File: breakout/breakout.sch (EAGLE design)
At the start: 34 parts, among them X1 PCIE-MINI-CONN

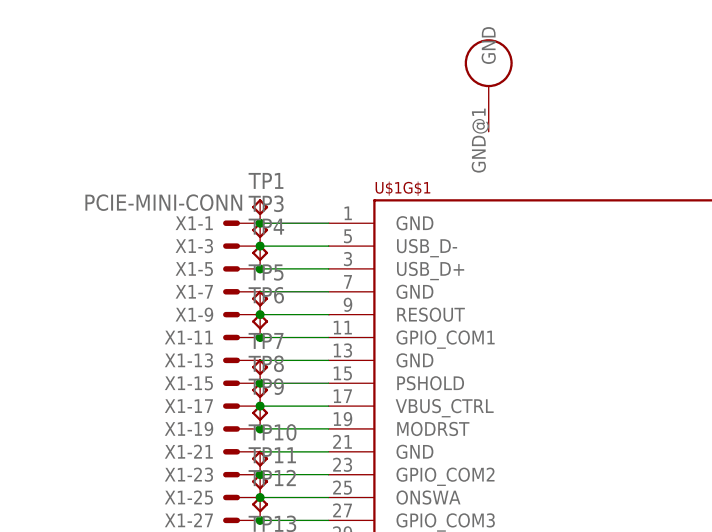
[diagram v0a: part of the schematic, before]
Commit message: Fix incorrect signal in breakout board
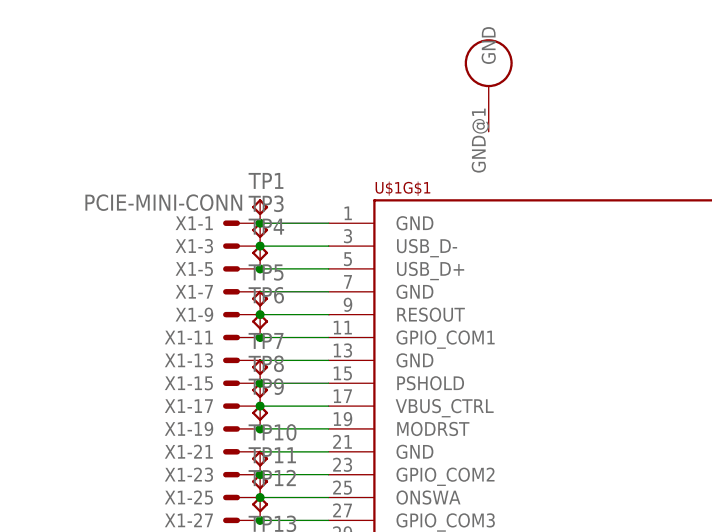
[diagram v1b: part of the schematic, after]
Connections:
- net USB_D+ renamed USB_P
- net USB_D- renamed USB_N
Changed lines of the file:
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@@
 </busses>
 <nets>
-<net name="USB_D-" class="0">
-<segment>
-<pinref part="X1" gate="-3" pin="S"/>
-<pinref part="U$1" gate="G$1" pin="USB_D-"/>
-<wire x1="25.4" y1="68.58" x2="33.02" y2="68.58" width="0.1524" layer="91"/>
-<pinref part="TP3" gate="G$1" pin="TP"/>
-<junction x="25.4" y="68.58"/>
-</segment>
-</net>
-<net name="USB_D+" class="0">
+<net name="USB_P" class="0">
 <segment>
 <pinref part="X1" gate="-5" pin="S"/>
+<pinref part="TP4" gate="G$1" pin="TP"/>
 <pinref part="U$1" gate="G$1" pin="USB_D+"/>
-<wire x1="25.4" y1="66.04" x2="33.02" y2="66.04" width="0.1524" layer="91"/>
-<pinref part="TP4" gate="G$1" pin="TP"/>
+<wire x1="33.02" y1="66.04" x2="25.4" y2="66.04" width="0.1524" layer="91"/>
 <junction x="25.4" y="66.04"/>
 </segment>
@@
 </segment>
 </net>
+<net name="USB_N" class="0">
+<segment>
+<pinref part="X1" gate="-3" pin="S"/>
+<pinref part="TP3" gate="G$1" pin="TP"/>
+<pinref part="U$1" gate="G$1" pin="USB_D-"/>
+<wire x1="33.02" y1="68.58" x2="25.4" y2="68.58" width="0.1524" layer="91"/>
+<junction x="25.4" y="68.58"/>
+</segment>
+</net>
